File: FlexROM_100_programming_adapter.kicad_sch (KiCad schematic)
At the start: 2 parts

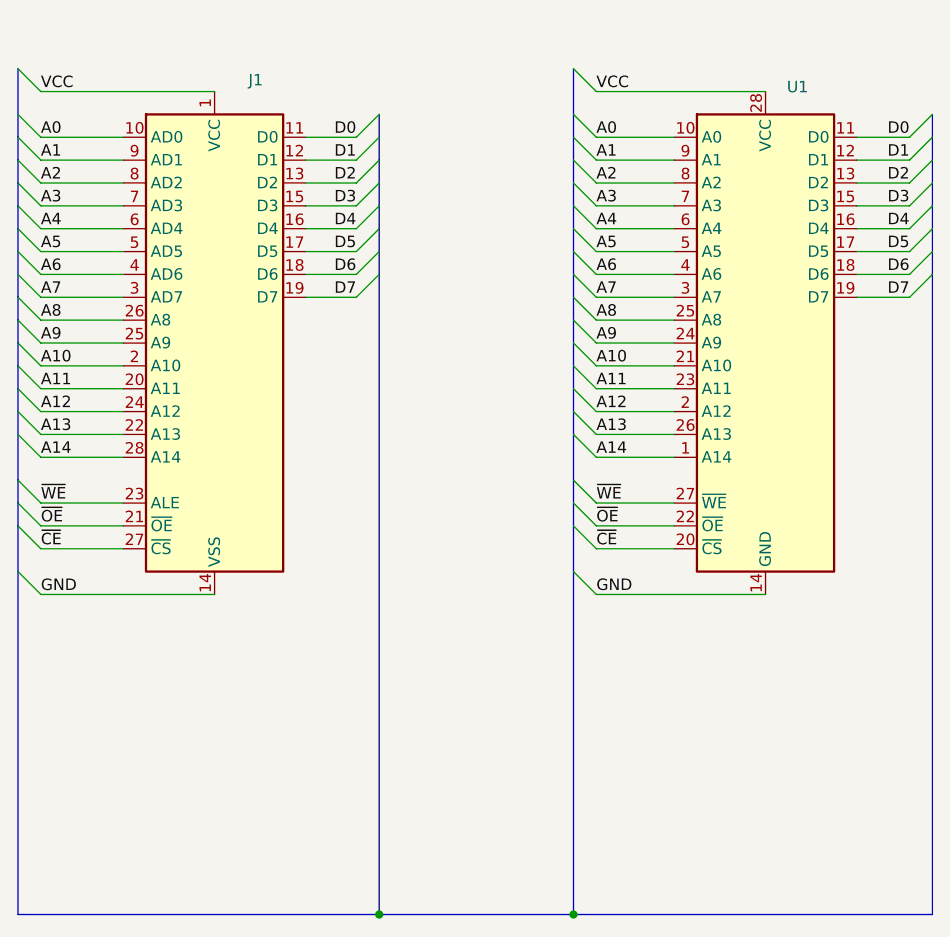
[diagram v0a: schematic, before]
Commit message: programming adapter board outline & ground pour
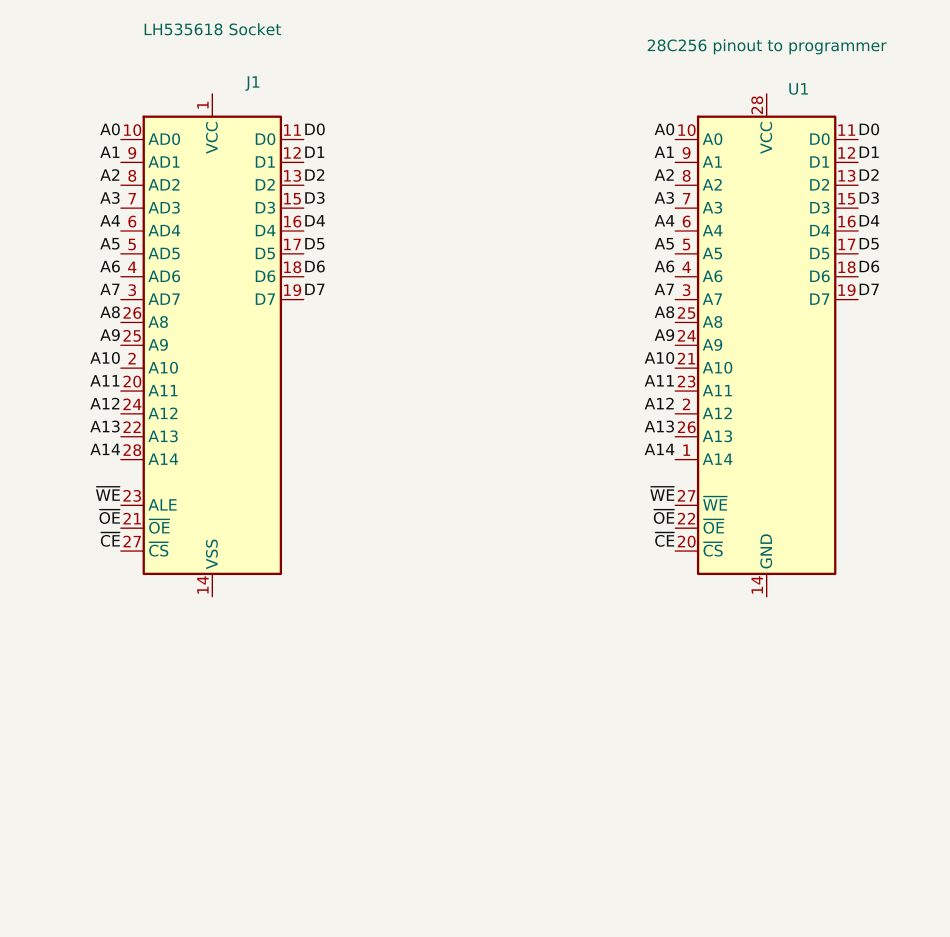
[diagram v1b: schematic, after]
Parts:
- J1: value (none) -> LH535618 Socket; footprint (none) -> 000_LOCAL:DIP28_0.6
- U1: value (none) -> 28C256 pinout to programmer; footprint (none) -> 000_LOCAL:2x28_0.3_0.1_pins
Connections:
- net GND: no longer names the net of U1.14 (GND)
- net GND: no longer J1.14 (VSS)
- net VCC: no longer names the net of U1.28 (VCC)
- net VCC: no longer J1.1 (VCC)
